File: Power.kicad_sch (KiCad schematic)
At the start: 46 parts, among them U10 TLV62569DDC, U11 TLV62569DDC, U12 TLV62569DDC, U9 TLV62569DDC

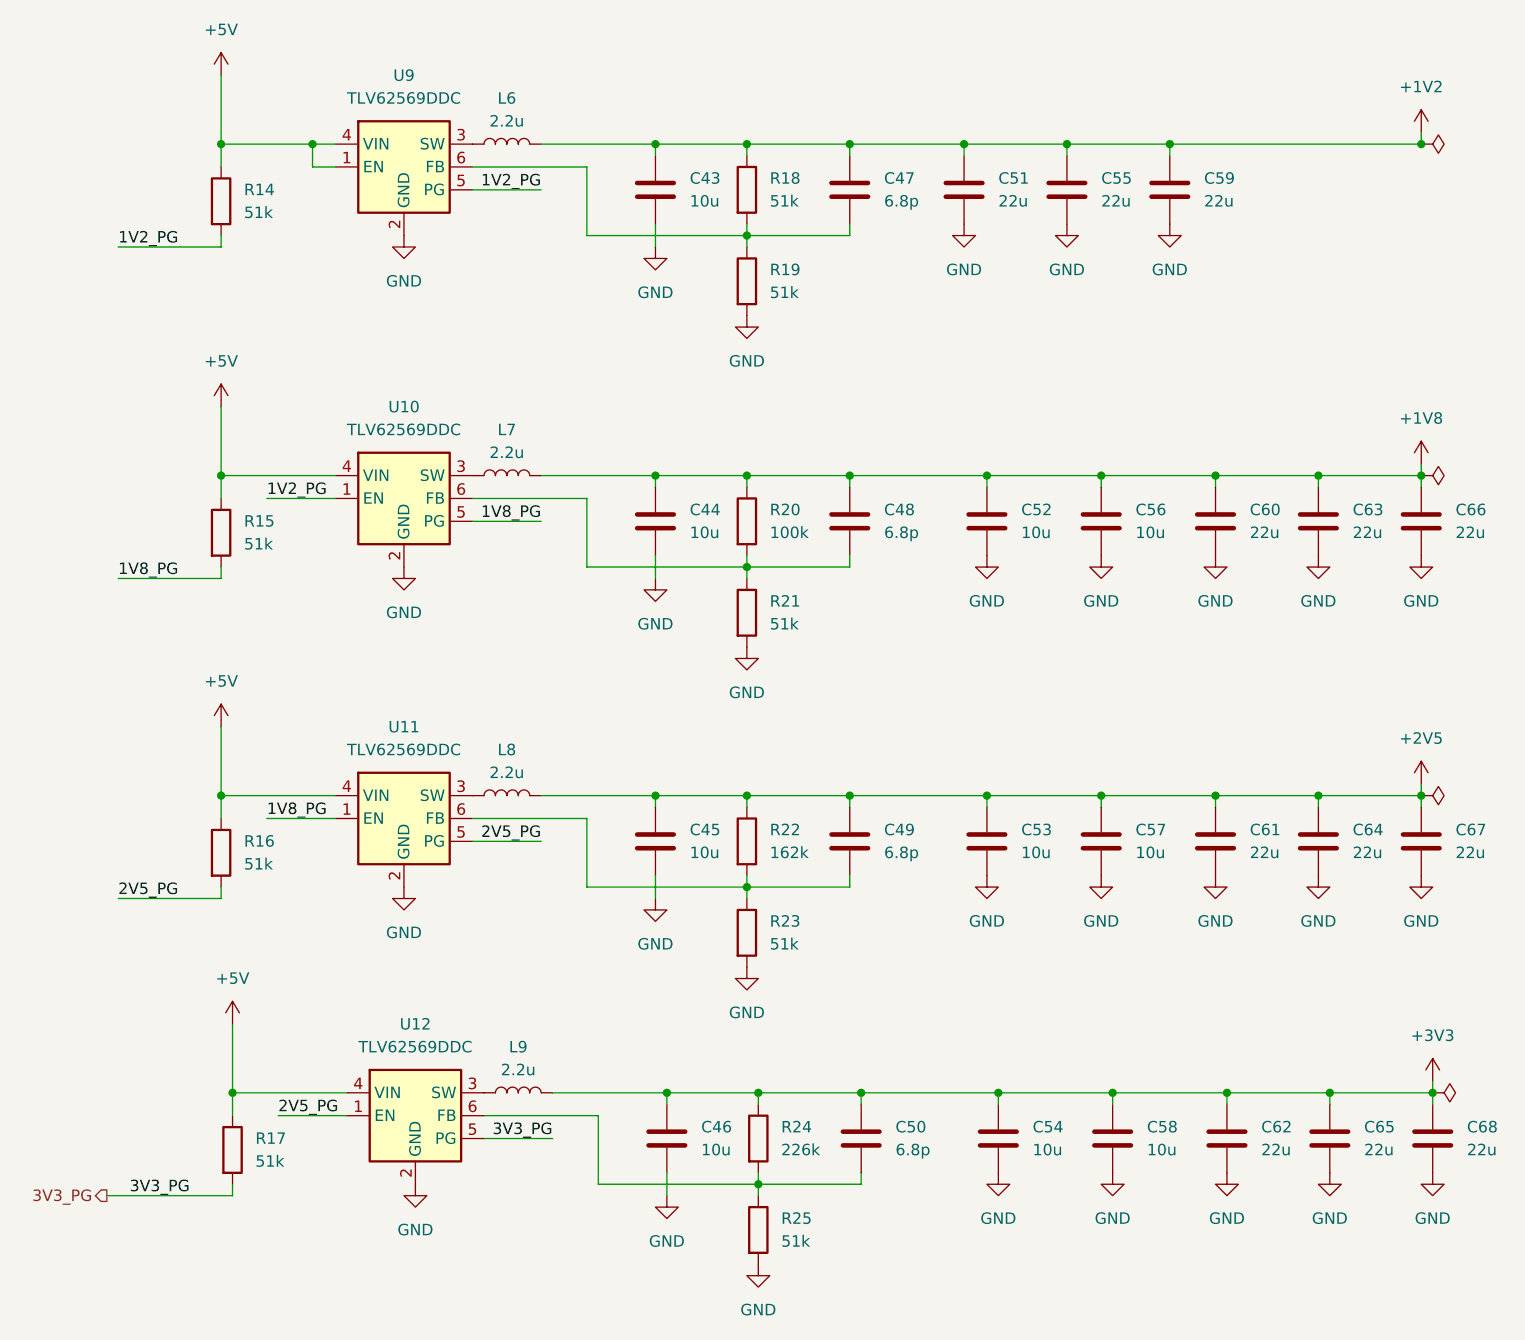
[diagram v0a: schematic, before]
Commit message: Fix SPI voltages, etc
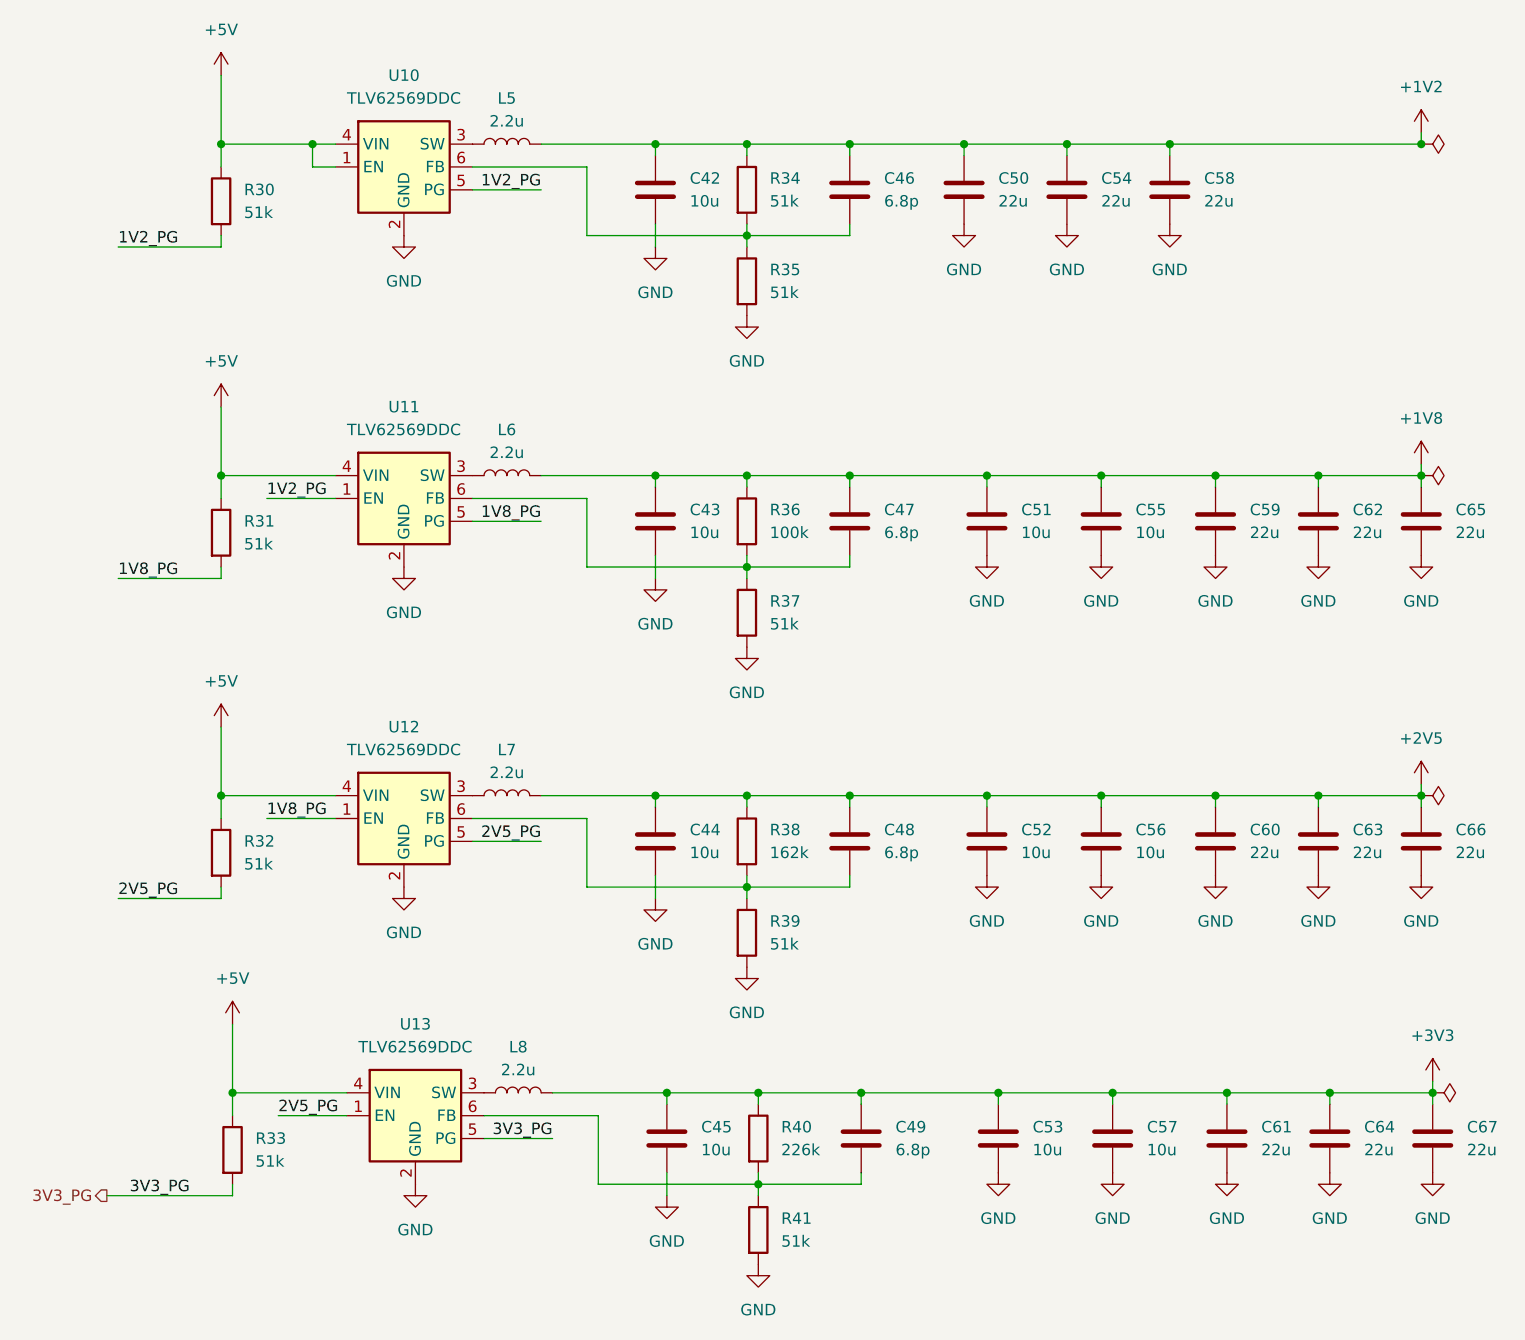
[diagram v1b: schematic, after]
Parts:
- renumbered C43 to C42, C44 to C43, C45 to C44, C46 to C45, C47 to C46, C48 to C47, C49 to C48, C50 to C49, C51 to C50, C52 to C51, C53 to C52, C54 to C53, C55 to C54, C56 to C55, C57 to C56, C58 to C57, C59 to C58, C60 to C59, C61 to C60, C62 to C61, C63 to C62, C64 to C63, C65 to C64, C66 to C65, C67 to C66, C68 to C67, L6 to L5, L7 to L6, L8 to L7, L9 to L8, R14 to R30, R15 to R31, R16 to R32, R17 to R33, R18 to R34, R19 to R35, R20 to R36, R21 to R37, R22 to R38, R23 to R39, R24 to R40, R25 to R41, U9 to U10, U10 to U11, U11 to U12, U12 to U13

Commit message: Fix ferrite, etc
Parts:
- renumbered C42 to C51, C43 to C52, C44 to C53, C45 to C54, C46 to C55, C47 to C56, C48 to C57, C49 to C58, C50 to C59, C51 to C60, C52 to C61, C53 to C62, C54 to C63, C55 to C64, C56 to C65, C57 to C66, C58 to C67, C59 to C68, C60 to C69, C61 to C70, C62 to C71, C63 to C72, C64 to C73, C65 to C74, C66 to C75, C67 to C76, R30 to R32, R31 to R33, R32 to R34, R33 to R35, R34 to R36, R35 to R37, R36 to R38, R37 to R39, R38 to R40, R39 to R41, R40 to R42, R41 to R43
